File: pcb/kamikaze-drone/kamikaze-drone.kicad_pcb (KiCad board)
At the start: 4 copper layers, 50.5 x 50 mm, 87 parts, among them J1 SWD Connector, J2 Battery Input, J3 16P_USB_C, J4 Conn_02x09_Odd_Even, M1 Brushless DC, M2 Brushless DC, M3 Brushless DC, M4 Brushless DC, Q1 SI2300DS, Q2 SI2300DS, Q3 SI2300DS, Q4 SI2300DS, SW1 SW_NRST, SW2 SW_BOOT0, U1 STM32F765VITx, U2 USBLC6-2P6, U3 MCP73871-2CC, U4 AMS1117-3.3, U5 LSM6DSL, U6 W25Q64JVSS, U7 BMP280, U8 VL53L1CXV0FY1, Y1 25 MHz

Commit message: New layout for pcb
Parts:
- C18, C19, C20, C22, C23, C26, D4, R11, R15, R16, U4, U5, U7: moved to F.Cu
- moved R12 239.9 mm to (-55.4, 8.36), turned to 0 degrees
- moved C21 237.8 mm to (-59.7, 5.85)
- moved R13 236.5 mm to (-55.4, 10.9), turned to 0 degrees
- moved R18 235.0 mm to (-51.0, 10.9), turned to 0 degrees
- moved R17 234.6 mm to (-51.0, 8.36), turned to 0 degrees
- moved C23 230.4 mm to (-59.7, 10.9)
- moved U6 230.3 mm to (-56.7, 18.2), turned to 0 degrees
- moved C26 230.1 mm to (-55.4, 5.85), turned to 0 degrees
- moved R14 226.6 mm to (-55.4, 13.4), turned to 0 degrees
- moved R15 223.6 mm to (-51.0, 3.34)
- moved U7 221.3 mm to (-59.7, 27.8), turned to 0 degrees
- moved C3 220.4 mm to (-44.5, 25.0)
- moved R16 219.4 mm to (-51.0, 5.85), turned to 0 degrees
- moved C4 217.2 mm to (-44.5, 28.0), turned to 0 degrees
- moved C20 216.2 mm to (-59.7, 3.34), turned to 0 degrees
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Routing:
- net GND: track 159.4 -> 0.00 mm, vias 31 -> 0
- net VBAT: track 152.6 -> 0.00 mm, vias 9 -> 0
- net +3V3: track 123.4 -> 0.00 mm, vias 43 -> 0
- net VBUS: track 66.4 -> 0.00 mm, vias 1 -> 0
- net I2C1_SCL: track 65.9 -> 0.00 mm, vias 1 -> 0
- net I2C1_SDA: track 57.9 -> 0.00 mm, vias 1 -> 0
- net SWD_NRST: track 52.6 -> 0.00 mm
- net I2C4_SCL: track 48.0 -> 0.00 mm
- net I2C4_SDA: track 45.4 -> 0.00 mm
- net DCMI_PCLK: track 43.4 -> 0.00 mm, vias 1 -> 0
- net DCMI_HSYNC: track 39.4 -> 0.00 mm, vias 2 -> 0
- net DCMI_D4: track 35.0 -> 0.00 mm, vias 1 -> 0
- net DCMI_D6: track 32.1 -> 0.00 mm, vias 2 -> 0
- net M2_SIG: track 30.0 -> 0.00 mm, vias 1 -> 0
- net DCMI_D7: track 29.4 -> 0.00 mm, vias 2 -> 0
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- removed copper zone on B.Cu, net +3V3
- removed copper zone on In2.Cu, net +3V3
- removed copper zone on B.Cu, net GND
- removed copper zone on In1.Cu, net GND
- removed copper zone on B.Cu, net VBAT
- removed copper zone on F.Cu, net VBAT
- removed copper zone on B.Cu, net VBUS
- removed copper zone on B.Cu, net VSYS
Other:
- board size 50.5 x 50 mm -> 50 x 50 mm

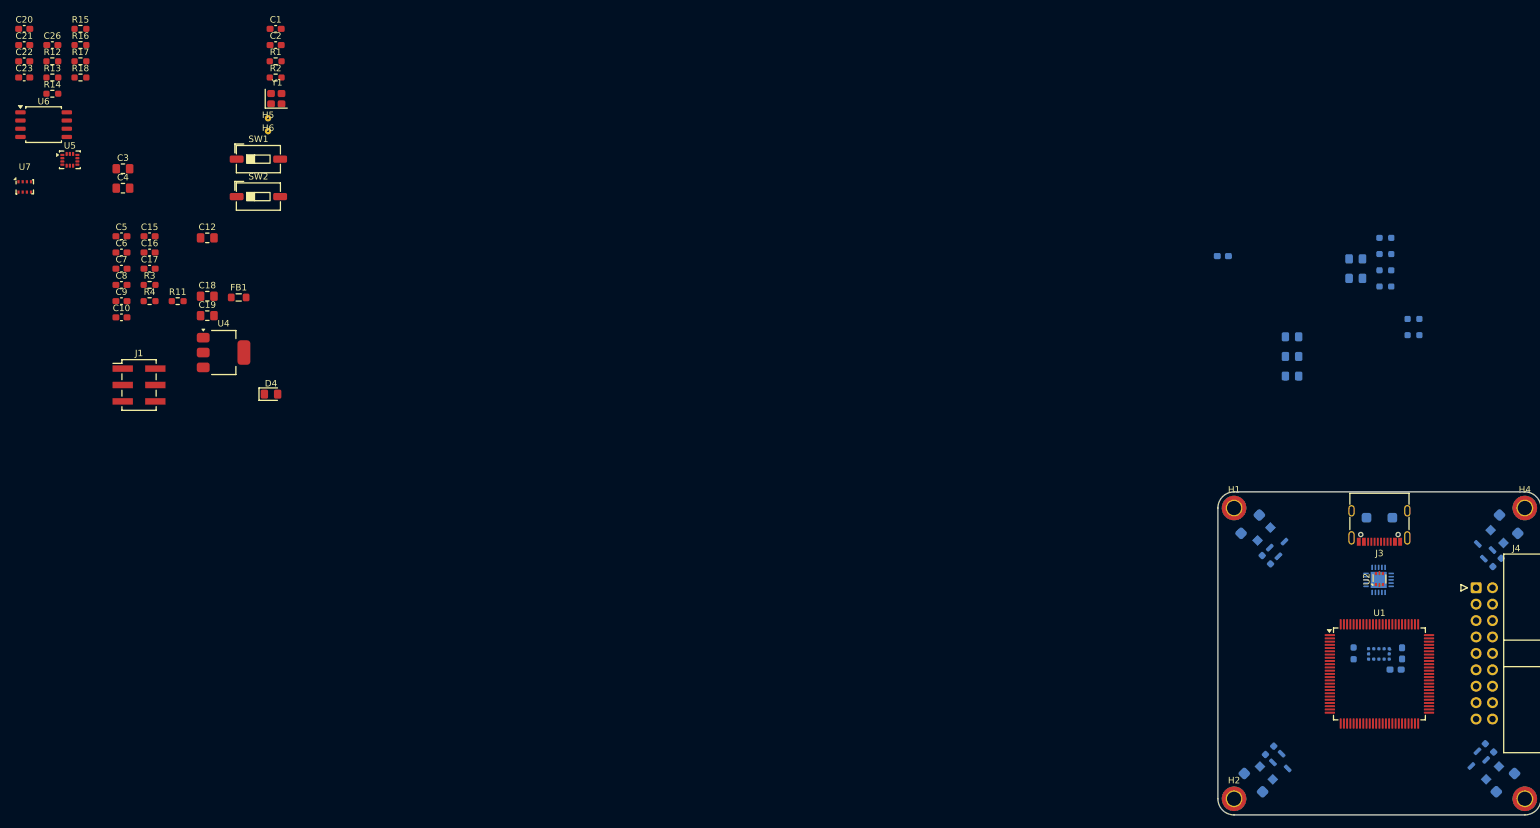
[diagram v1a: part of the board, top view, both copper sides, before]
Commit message: WIP - arranging components in updated PCB
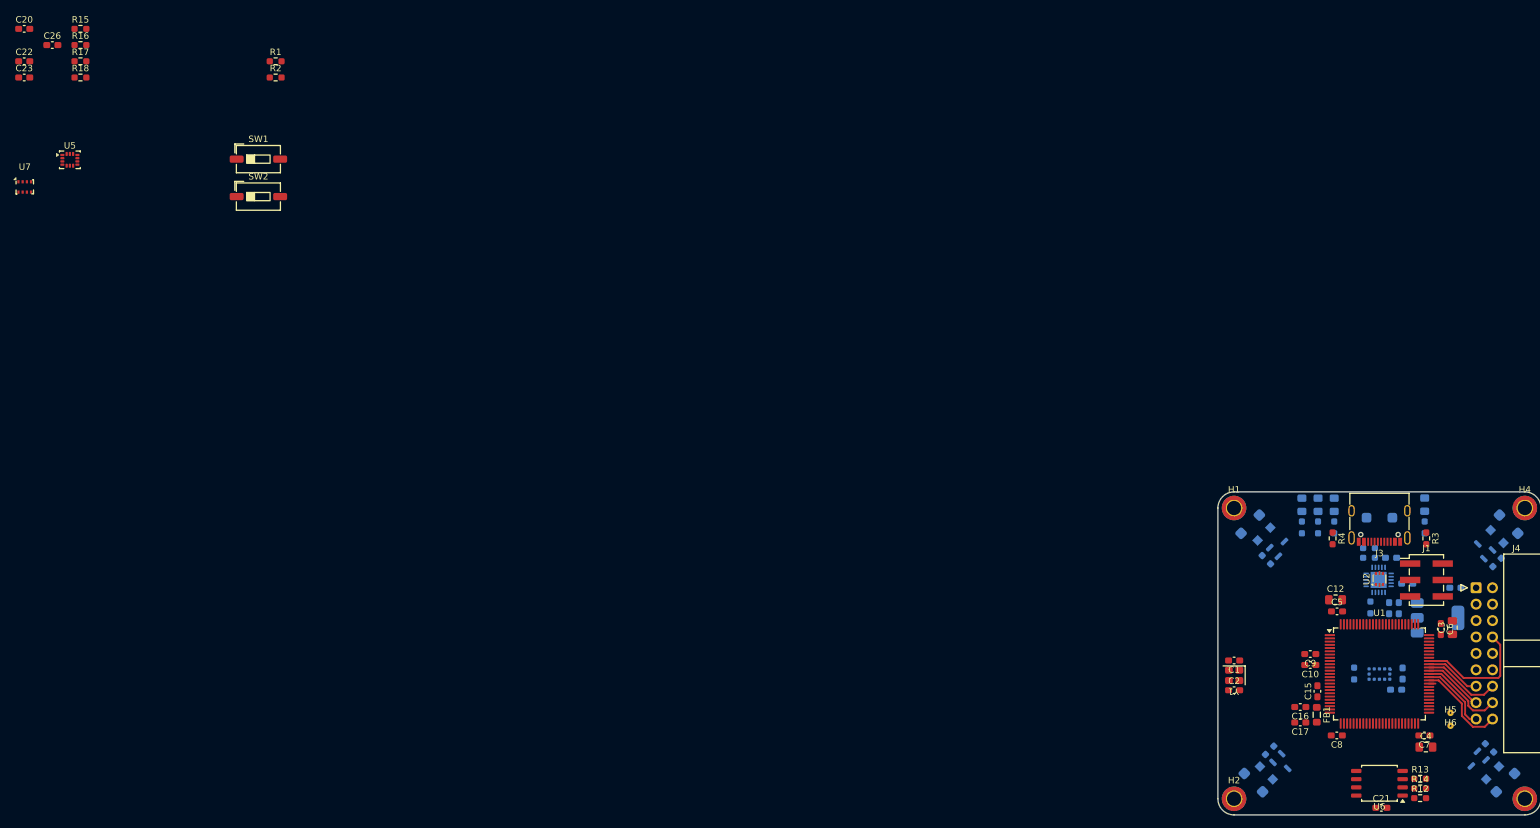
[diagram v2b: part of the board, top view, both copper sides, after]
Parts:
- C13, C14: footprint Capacitor_SMD:C_0805_2012Metric_Pad1.18x1.45mm_HandSolder -> Capacitor_SMD:C_0603_1608Metric_Pad1.08x0.95mm_HandSolder
- C18, C19: footprint Capacitor_SMD:C_0805_2012Metric_Pad1.18x1.45mm_HandSolder -> Capacitor_SMD:C_0603_1608Metric_Pad1.08x0.95mm_HandSolder; moved to B.Cu
- D4, R11, U4: moved to B.Cu
- moved C21 240.9 mm to (150.3, 123.9)
- moved R12 240.5 mm to (156.3, 122.4)
- moved R13 237.9 mm to (156.3, 119.4)
- moved R14 237.4 mm to (156.3, 120.9)
- moved U6 230.5 mm to (150.0, 120.1), turned to 180 degrees
- moved C4 219.4 mm to (157.2, 114.5)
- moved C3 217.7 mm to (161.3, 96.0), turned to 90 degrees
- moved C7 214.2 mm to (157.0, 112.7), turned to 180 degrees
- moved C6 212.3 mm to (159.5, 96.2), turned to -90 degrees
- moved H5 204.8 mm to (161.0, 109.2)
- moved H6 204.8 mm to (161.0, 111.2)
- moved J1 201.5 mm to (157.3, 88.6)
- moved R3 201.4 mm to (157.2, 82.2), turned to -90 degrees
- moved C8 200.6 mm to (143.4, 112.7), turned to 180 degrees
- moved C19 197.7 mm to (161.8, 89.8), turned to 180 degrees
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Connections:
- U1 pad 61: DCMI_RST -> DCMI_PDWN
- U1 pad 62: DCMI_PDWN -> DCMI_RST
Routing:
- net DCMI_XCLK: track 0.00 -> 18.8 mm
- net DCMI_PDWN: track 0.00 -> 14.4 mm
- net DCMI_D0: track 0.00 -> 13.1 mm
- net DCMI_D2: track 0.00 -> 12.1 mm
- net DCMI_RST: track 0.00 -> 11.1 mm
- net DCMI_D1: track 0.00 -> 9.51 mm
- net DCMI_D3: track 0.00 -> 8.70 mm
- net I2C4_SDA: track 0.00 -> 1.00 mm

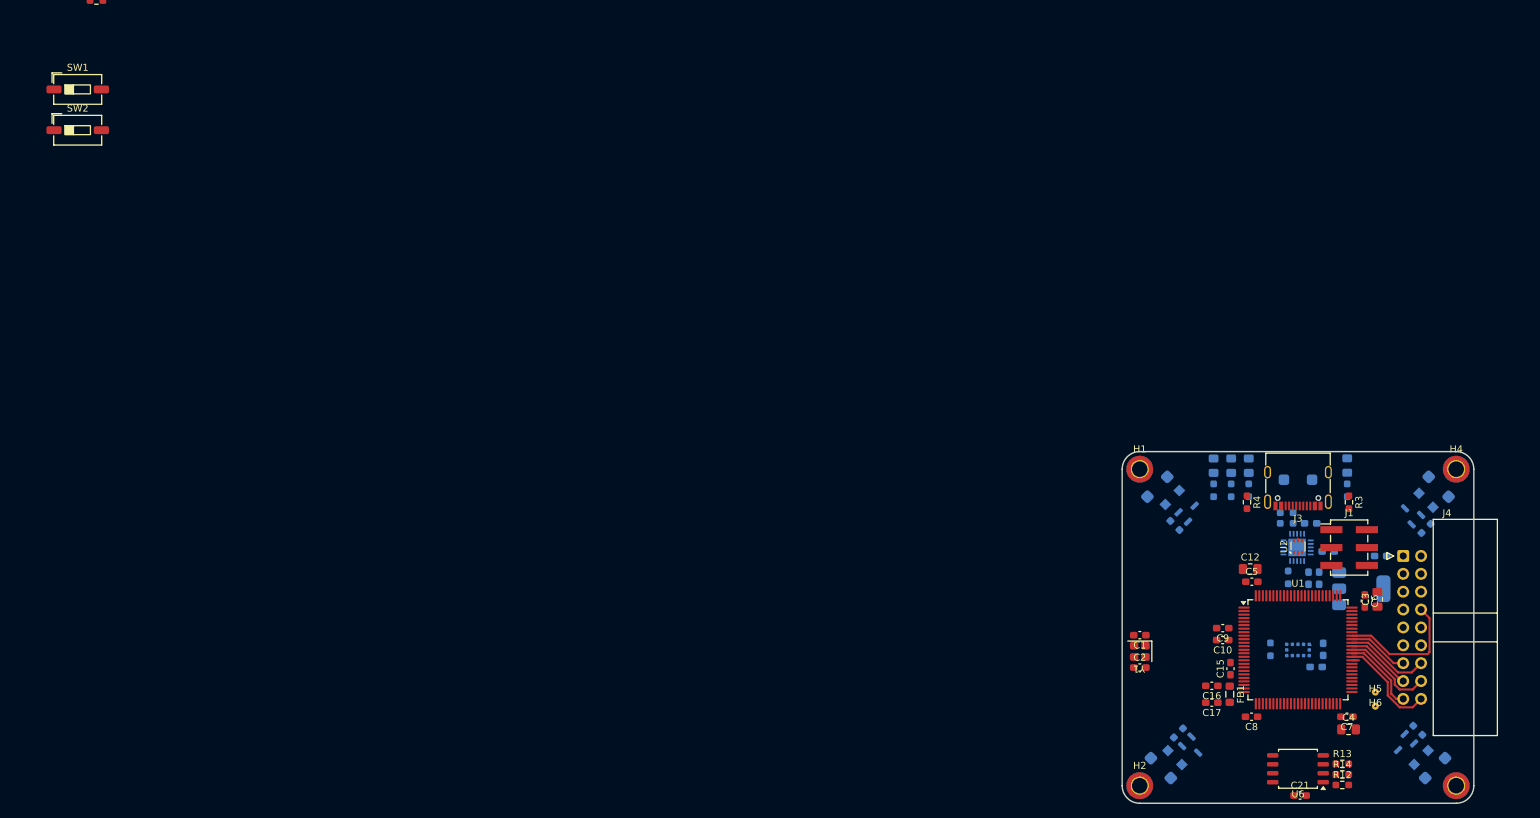
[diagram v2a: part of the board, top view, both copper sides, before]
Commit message: WIP - Power routing done. Signal routing remaining
- Power routing from USB and battery to MCP and AMS completed.
- Power routing from motors to battery completed
- Grounds have not been routed yet, leaving to the end.
- Most 3V3 pads haven't been routed yet, leaving to the end
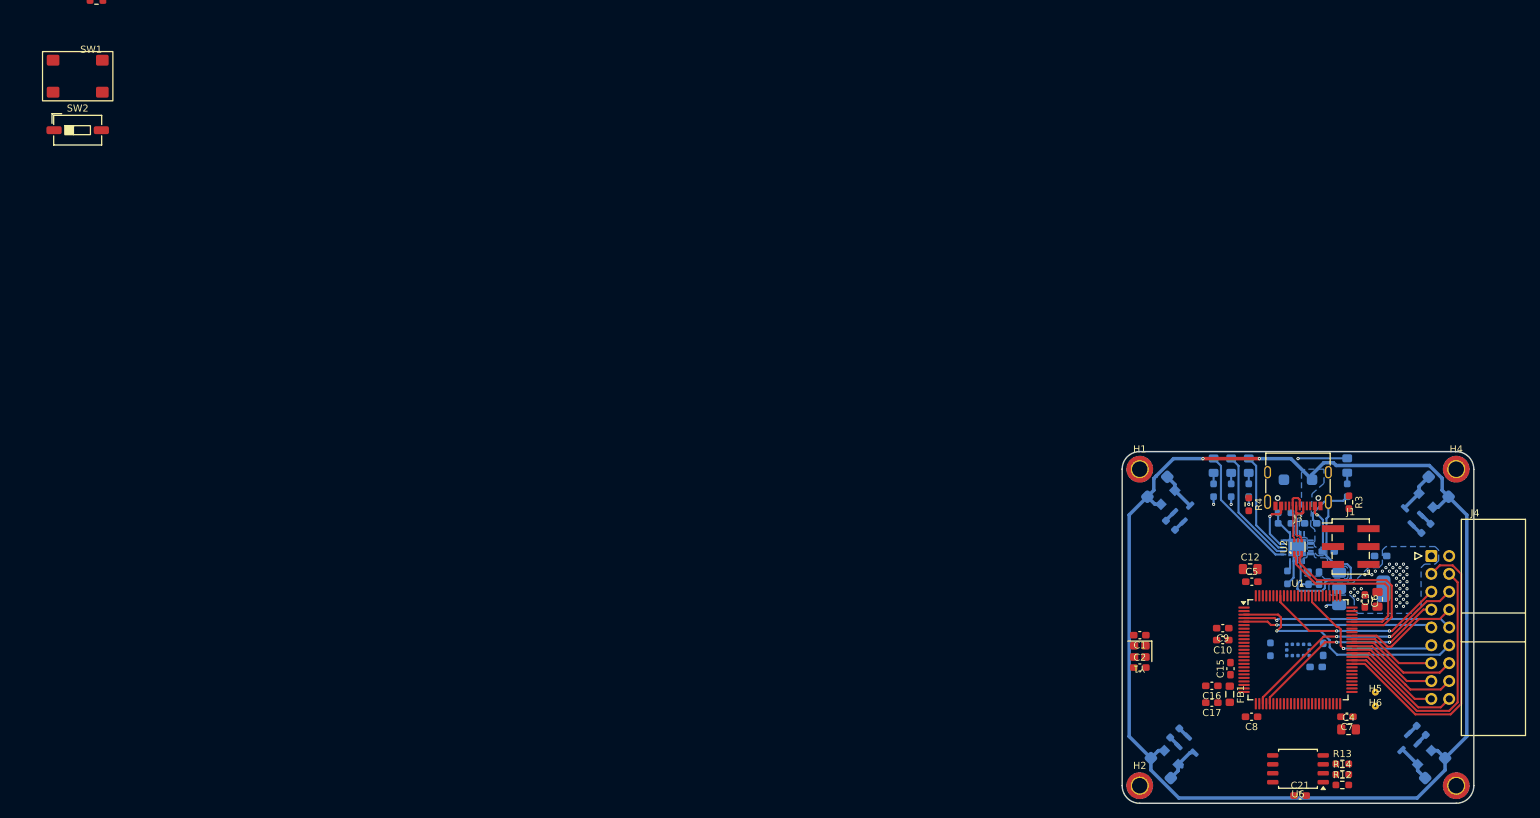
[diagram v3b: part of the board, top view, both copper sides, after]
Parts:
- SW1: footprint Button_Switch_SMD:SW_DIP_SPSTx01_Slide_6.7x4.1mm_W6.73mm_P2.54mm_LowProfile_JPin -> kamikaze_drone_custom_footprints:button-footprint
- moved J4 4.00 mm to (169.0, 89.8)
- moved SW1 1.88 mm to (-23.5, 21.6)
- moved D5 0.63 mm to (131.5, 81.5)
- moved Q1 0.63 mm to (133.9, 83.5)
- moved R20 0.63 mm to (131.9, 85.5)
- moved D7 0.52 mm to (132.0, 118.5)
- moved Q3 0.52 mm to (134.5, 117.0)
- moved R22 0.52 mm to (132.5, 115.0)
- moved D8 0.49 mm to (168.0, 118.5)
- moved Q4 0.49 mm to (165.5, 116.6)
- moved R23 0.49 mm to (167.5, 114.6)
- moved R4 0.39 mm to (143.0, 82.5)
- moved R5 0.30 mm to (148.1, 85.2)
- moved R6 0.30 mm to (148.1, 83.7)
- moved J1 0.26 mm to (157.5, 88.5)
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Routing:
- net VBAT: track 0.00 -> 189.2 mm, vias 0 -> 2
- net I2C4_SCL: track 0.00 -> 42.8 mm
- net GND: track 0.00 -> 41.4 mm, vias 0 -> 2
- net I2C4_SDA: track 1.00 -> 37.3 mm
- net DCMI_D4: track 0.00 -> 34.6 mm, vias 0 -> 1
- net VBUS: track 0.00 -> 34.4 mm, vias 0 -> 2
- net DCMI_HSYNC: track 0.00 -> 33.6 mm, vias 0 -> 2
- net DCMI_D6: track 0.00 -> 29.9 mm, vias 0 -> 1
- net DCMI_PCLK: track 0.00 -> 29.0 mm, vias 0 -> 2
- net DCMI_D7: track 0.00 -> 27.0 mm, vias 0 -> 1
- net USB_D-: track 0.00 -> 26.7 mm
- net DCMI_VSYNC: track 0.00 -> 26.4 mm, vias 0 -> 2
- net USB_D+: track 0.00 -> 25.8 mm
- net DCMI_D5: track 0.00 -> 22.2 mm, vias 0 -> 1
- net MCP_PG: track 0.00 -> 18.4 mm
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- added copper zone on B.Cu, net +3V3
- added copper zone on In2.Cu, net +3V3
- added copper zone on In1.Cu, net GND
- added copper zone on B.Cu, net VBAT
- added copper zone on B.Cu, net VBUS
- added copper zone on B.Cu, net VSYS

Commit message: v2.0 of PCB completed
Updated routing to have USB port in center of top.
Shrank overall size to 50x50 mm
Layout is now ground+signal >> ground >> 3V3 >> signal

TODO: Add stitching vias between ground on top and second layer?
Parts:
- 25 MHz: renamed from Y1
- C20, C22, R15, R16, R17, R18, U5: moved to B.Cu
- moved R17 229.8 mm to (156.3, 107.4), turned to -90 degrees
- moved R18 227.3 mm to (154.7, 107.4), turned to -90 degrees
- moved C26 220.1 mm to (134.5, 117.1), turned to -90 degrees
- moved C23 220.0 mm to (132.9, 117.1), turned to -90 degrees
- moved R15 218.8 mm to (145.7, 99.1), turned to 90 degrees
- moved R16 214.8 mm to (142.5, 99.1), turned to 90 degrees
- moved C22 212.2 mm to (128.6, 106.2)
- moved C20 212.0 mm to (128.6, 100.7)
- moved U7 211.7 mm to (133.7, 114.1)
- moved U5 198.1 mm to (128.6, 103.4), turned to 90 degrees
- moved R2 179.1 mm to (136.5, 96.5)
- moved R1 175.1 mm to (130.3, 96.8)
- moved BOOT0 171.4 mm to (136.5, 90.9), turned to 90 degrees
- moved NRST 168.6 mm to (130.2, 90.9), turned to 90 degrees
- moved R14 12.9 mm to (143.4, 120.7), turned to 180 degrees
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- renumbered SW2 to BOOT0, J2 to Battery, SW1 to NRST, J4 to OVCAM, H5 to Payload, H6 to Return, J1 to SWD, J3 to USB-C
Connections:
- C3 pad 1: Net-(U1-VCAP_1) -> Net-(U1-VCAP_2)
- C4 pad 1: Net-(U1-VCAP_2) -> Net-(U1-VCAP_1)
- SWD pad 4: SWD_IO -> SWD_CLK
- SWD pad 6: SWD_CLK -> SWD_IO
- U1 pad 79: unconnected-(U1-PC11-Pad79) -> QSPI_NCS
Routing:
- net GND: track 41.4 -> 143.0 mm, vias 2 -> 21
- net +3V3: track 10.3 -> 104.7 mm, vias 46 -> 64
- net I2C1_SDA: track 0.00 -> 66.5 mm, vias 0 -> 2
- net SWD_NRST: track 0.00 -> 56.6 mm
- net I2C1_SCL: track 0.00 -> 45.2 mm, vias 0 -> 2
- net QSPI_NCS: track 0.00 -> 32.5 mm, vias 0 -> 4
- net M1_SIG: track 1.71 -> 24.7 mm, vias 0 -> 1
- net M2_SIG: track 1.88 -> 24.7 mm, vias 0 -> 1
- net M3_SIG: track 1.71 -> 22.5 mm, vias 0 -> 1
- net BOOT0: track 0.00 -> 17.1 mm
- net M4_SIG: track 1.71 -> 18.5 mm, vias 0 -> 1
- net QSPI_IO3: track 0.00 -> 16.1 mm, vias 0 -> 2
- net Net-(U1-PH1): track 0.00 -> 14.2 mm
- net SWD_O: track 0.00 -> 13.8 mm
- net QSPI_IO2: track 0.00 -> 13.3 mm
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- added copper zone on F.Cu, net GND
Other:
- board text added: "CLK"
- board text added: "DIO"
- board text added: "GND"
- board text added: "Kamikaze Drone Control Board v2"
- board text added: "NRST"
- board text added: "SWO"
- board text added: "VREF"

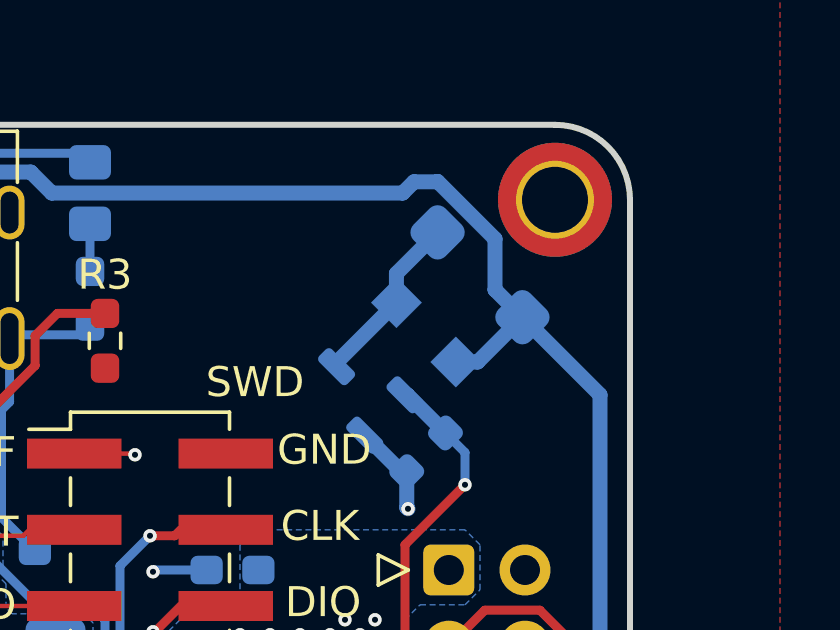
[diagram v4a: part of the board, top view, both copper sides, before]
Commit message: add: added watermark to pcb
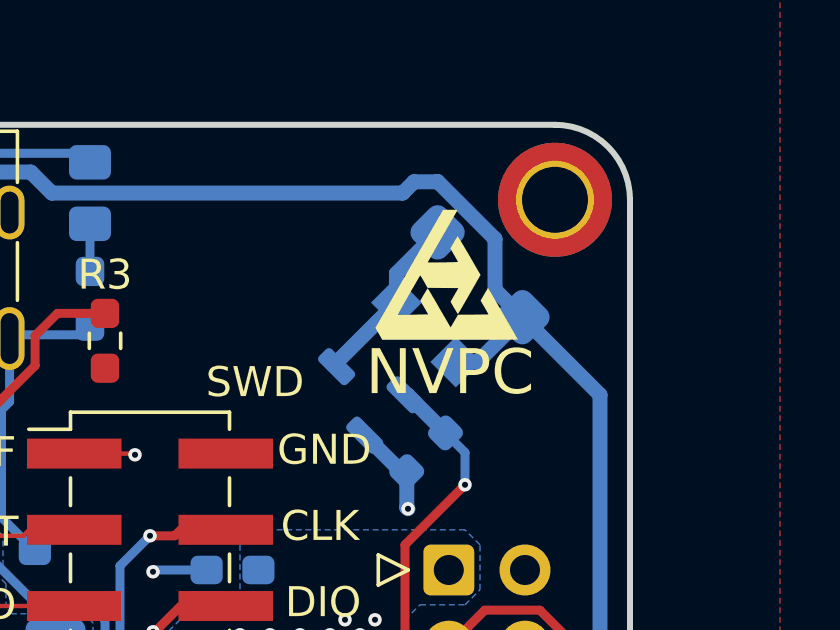
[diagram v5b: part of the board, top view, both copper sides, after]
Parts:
- added NVPC: LOGO, pranavs-footprints:logo, F.Cu at (169.0, 80.0)
